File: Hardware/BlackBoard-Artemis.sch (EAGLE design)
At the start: 84 parts, among them IC3 LM1117, J2 CORTEX_DEBUG, J3 POWER_JACKTOE, J5 USB-C, Q1 1.1A/60V/600mΩ, U3 AP2112-3.3V, U4 ARTEMIS_MODULESMD, U5 CH340C, Y1 32.768kHz

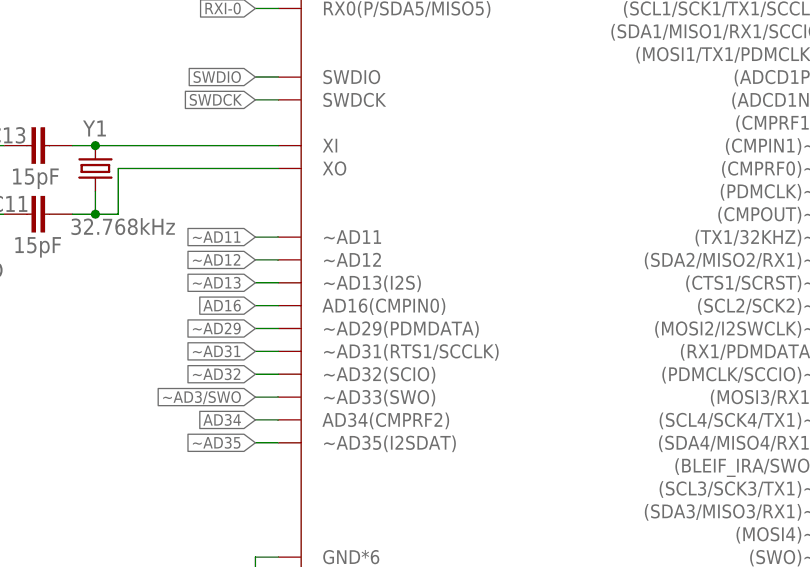
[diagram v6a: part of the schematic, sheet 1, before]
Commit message: Update silk on Artemis FP
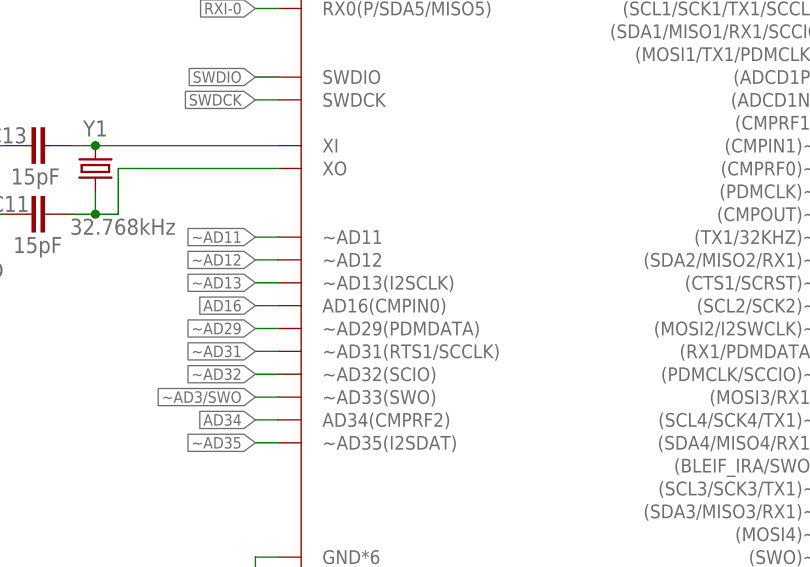
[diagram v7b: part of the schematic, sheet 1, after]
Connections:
- net ~AD13: now also U4.~AD13(I2SCLK); no longer U4.~AD13(I2S)
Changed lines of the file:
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@@
 </segment>
 <segment>
-<pinref part="U4" gate="G$1" pin="~AD13(I2S)"/>
+<pinref part="U4" gate="G$1" pin="~AD13(I2SCLK)"/>
 <wire x1="314.96" y1="114.3" x2="312.42" y2="114.3" width="0.1524" layer="91"/>
 <label x="312.42" y="114.3" size="1.27" layer="95" rot="R180" xref="yes"/>
